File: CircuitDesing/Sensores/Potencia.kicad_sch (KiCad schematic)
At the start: 5 parts

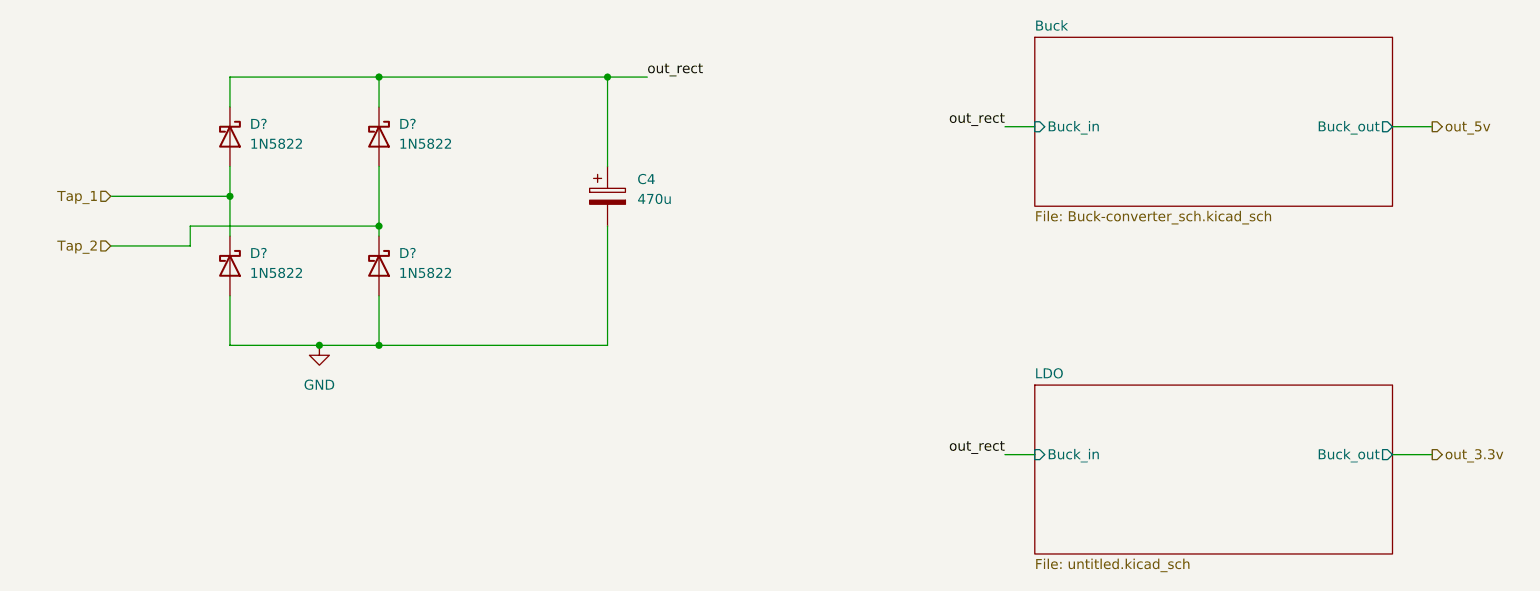
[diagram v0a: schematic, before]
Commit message: Modificaciones generales
Modificaciones a esquemático,  interacción con otros grupos, sistema de potencia.
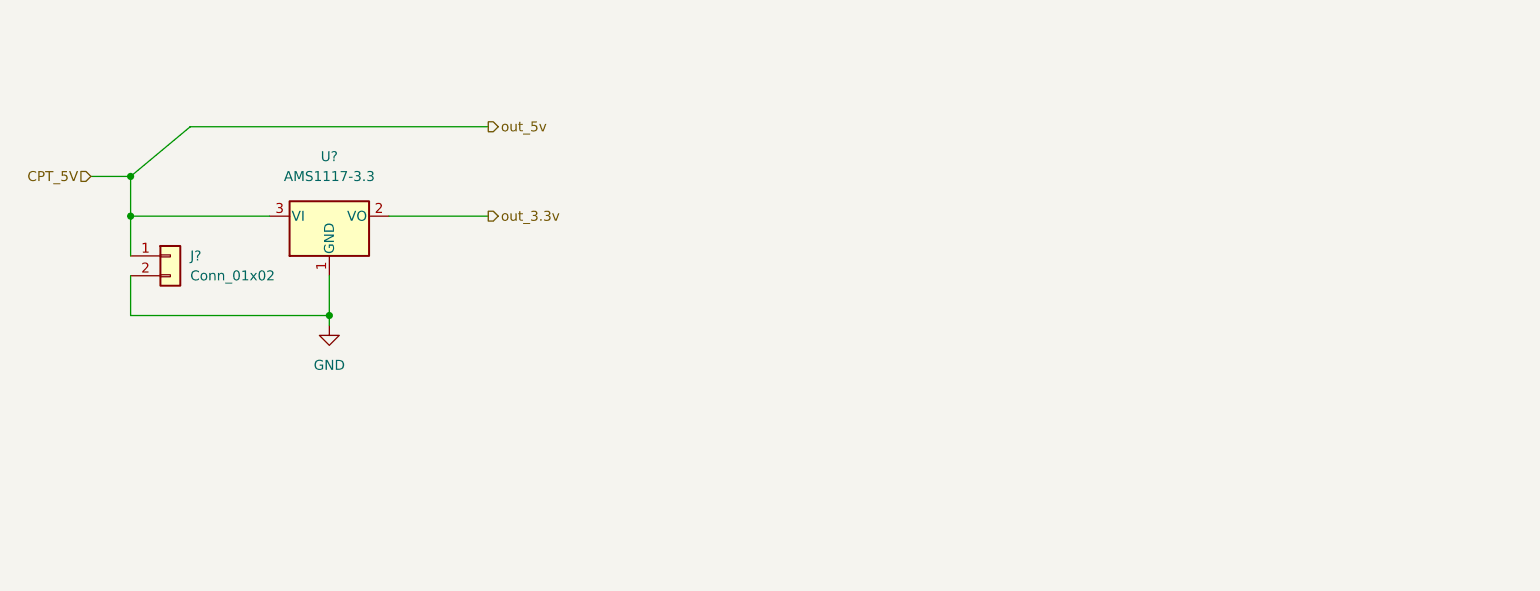
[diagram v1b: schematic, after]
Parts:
- removed C4: 470u, symbol Device:C_Polarized
- removed D? (x4): 1N5822, Diode_THT:D_DO-201AD_P15.24mm_Horizontal, symbol Diode:1N5822
- added J?: Conn_01x02, symbol Connector_Generic:Conn_01x02
- added U?: AMS1117-3.3, Package_TO_SOT_SMD:SOT-223-3_TabPin2, symbol Regulator_Linear:AMS1117-3.3
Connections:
- net GND: now also J?.2 (Pin_2), U?.1 (GND)
- net out_3.3v: now also U?.2 (VO)
- new net CPT_5V: J?.1 (Pin_1), U?.3 (VI)
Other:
- removed sheet Buck
- removed sheet LDO

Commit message: Huellas
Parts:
- J1: renamed from J?; footprint (none) -> TerminalBlock:TerminalBlock_bornier-2_P5.08mm
- gave numbers to parts that had none: 1
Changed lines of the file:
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@@
   (symbol (lib_id "Connector_Generic:Conn_01x02") (at 59.69 73.66 0) (unit 1)
     (in_bom yes) (on_board yes) (fields_autoplaced)
-    (property "Reference" "J?" (id 0) (at 62.23 73.6599 0)
+    (property "Reference" "J1" (id 0) (at 62.23 73.6599 0)
       (effects (font (size 1.27 1.27)) (justify left))
     )
@@
       (effects (font (size 1.27 1.27)) (justify left))
     )
-    (property "Footprint" "" (id 2) (at 59.69 73.66 0)
+    (property "Footprint" "TerminalBlock:TerminalBlock_bornier-2_P5.08mm" (id 2) (at 59.69 73.66 0)
       (effects (font (size 1.27 1.27)) hide)
     )
@@
   (symbol (lib_id "Regulator_Linear:AMS1117-3.3") (at 80.01 68.58 0) (unit 1)
     (in_bom yes) (on_board yes) (fields_autoplaced)
-    (property "Reference" "U?" (id 0) (at 80.01 60.96 0))
+    (property "Reference" "U2" (id 0) (at 80.01 60.96 0))
     (property "Value" "AMS1117-3.3" (id 1) (at 80.01 63.5 0))
     (property "Footprint" "Package_TO_SOT_SMD:SOT-223-3_TabPin2" (id 2) (at 80.01 63.5 0)
@@
   (symbol (lib_id "power:GND") (at 80.01 82.55 0) (unit 1)
     (in_bom yes) (on_board yes) (fields_autoplaced)
-    (property "Reference" "#PWR?" (id 0) (at 80.01 88.9 0)
+    (property "Reference" "#PWR0110" (id 0) (at 80.01 88.9 0)
       (effects (font (size 1.27 1.27)) hide)
     )

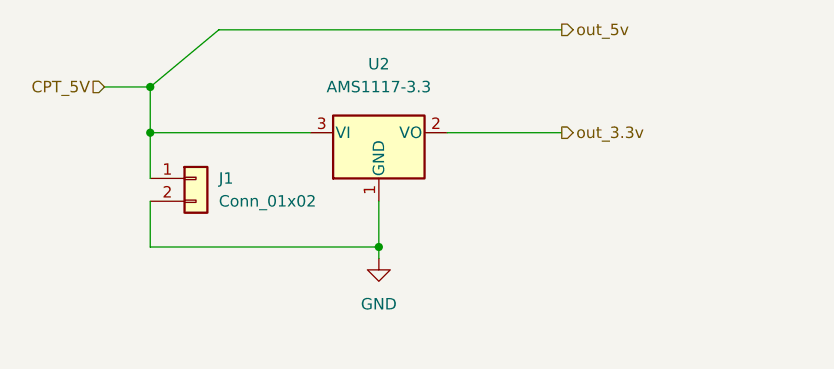
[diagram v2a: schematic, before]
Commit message: Condensadores LDO
Condensadores LDO
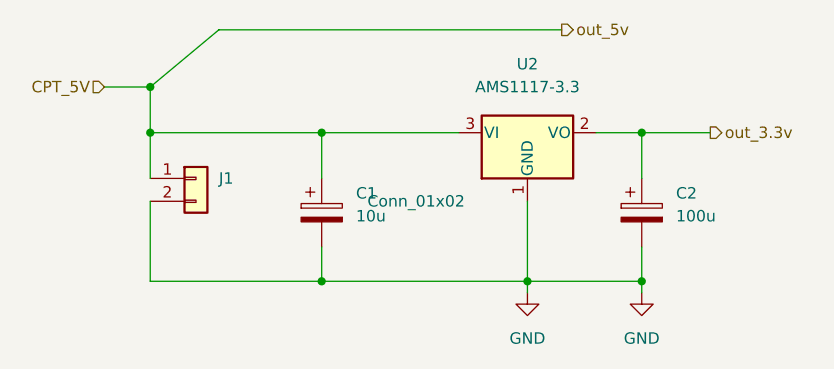
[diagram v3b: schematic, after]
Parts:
- added C1: 10u, Capacitor_SMD:C_0603_1608Metric_Pad1.08x0.95mm_HandSolder, symbol Device:C_Polarized
- added C2: 100u, Capacitor_SMD:C_0603_1608Metric_Pad1.08x0.95mm_HandSolder, symbol Device:C_Polarized
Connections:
- net CPT_5V: now also C1.1
- net GND: now also C1.2, C2.2
- net out_3.3v: now also C2.1
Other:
- moved on the sheet: U2
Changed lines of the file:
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@@
 (kicad_sch (version 20211123) (generator eeschema)
   (paper "A4")
-  (junction (at 80.01 81.28) (diameter 0) (color 0 0 0 0)
+  (junction (at 109.22 85.09) (diameter 0) (color 0 0 0 0)
   )
   (junction (at 54.61 63.5) (diameter 0) (color 0 0 0 0)
   )
+  (junction (at 73.66 68.58) (diameter 0) (color 0 0 0 0)
+  )
+  (junction (at 96.52 85.09) (diameter 0) (color 0 0 0 0)
+  )
+  (junction (at 73.66 85.09) (diameter 0) (color 0 0 0 0)
+  )
+  (junction (at 109.22 68.58) (diameter 0) (color 0 0 0 0)
+  )
   (junction (at 54.61 68.58) (diameter 0) (color 0 0 0 0)
   )
-  (wire (pts (xy 54.61 68.58) (xy 72.39 68.58))
+  (wire (pts (xy 96.52 76.2) (xy 96.52 85.09))
     (stroke (width 0) (type default) (color 0 0 0 0))
   )
-  (wire (pts (xy 80.01 76.2) (xy 80.01 81.28))
+  (wire (pts (xy 109.22 68.58) (xy 116.84 68.58))
     (stroke (width 0) (type default) (color 0 0 0 0))
   )
-  (wire (pts (xy 54.61 76.2) (xy 54.61 81.28))
+  (wire (pts (xy 54.61 76.2) (xy 54.61 85.09))
     (stroke (width 0) (type default) (color 0 0 0 0))
   )
-  (wire (pts (xy 80.01 81.28) (xy 54.61 81.28))
+  (wire (pts (xy 54.61 68.58) (xy 73.66 68.58))
+    (stroke (width 0) (type default) (color 0 0 0 0))
+  )
+  (wire (pts (xy 73.66 85.09) (xy 54.61 85.09))
+    (stroke (width 0) (type default) (color 0 0 0 0))
+  )
+  (wire (pts (xy 73.66 68.58) (xy 88.9 68.58))
     (stroke (width 0) (type default) (color 0 0 0 0))
   )
@@
     (stroke (width 0) (type default) (color 0 0 0 0))
   )
-  (wire (pts (xy 87.63 68.58) (xy 100.33 68.58))
+  (wire (pts (xy 109.22 68.58) (xy 109.22 73.66))
+    (stroke (width 0) (type default) (color 0 0 0 0))
+  )
+  (wire (pts (xy 96.52 85.09) (xy 96.52 86.36))
+    (stroke (width 0) (type default) (color 0 0 0 0))
+  )
+  (wire (pts (xy 104.14 68.58) (xy 109.22 68.58))
+    (stroke (width 0) (type default) (color 0 0 0 0))
+  )
+  (wire (pts (xy 73.66 68.58) (xy 73.66 73.66))
     (stroke (width 0) (type default) (color 0 0 0 0))
   )
   (wire (pts (xy 54.61 68.58) (xy 54.61 73.66))
-    (stroke (width 0) (type default) (color 0 0 0 0))
-  )
-  (wire (pts (xy 80.01 81.28) (xy 80.01 82.55))
     (stroke (width 0) (type default) (color 0 0 0 0))
   )
@@
   )
   (wire (pts (xy 62.23 57.15) (xy 54.61 63.5))
+    (stroke (width 0) (type default) (color 0 0 0 0))
+  )
+  (wire (pts (xy 109.22 85.09) (xy 109.22 81.28))
+    (stroke (width 0) (type default) (color 0 0 0 0))
+  )
+  (wire (pts (xy 96.52 85.09) (xy 109.22 85.09))
+    (stroke (width 0) (type default) (color 0 0 0 0))
+  )
+  (wire (pts (xy 109.22 86.36) (xy 109.22 85.09))
+    (stroke (width 0) (type default) (color 0 0 0 0))
+  )
+  (wire (pts (xy 73.66 85.09) (xy 96.52 85.09))
+    (stroke (width 0) (type default) (color 0 0 0 0))
+  )
+  (wire (pts (xy 73.66 81.28) (xy 73.66 85.09))
     (stroke (width 0) (type default) (color 0 0 0 0))
   )
@@
     (effects (font (size 1.27 1.27)) (justify left))
   )
-  (hierarchical_label "out_3.3v" (shape output) (at 100.33 68.58 0)
+  (hierarchical_label "out_3.3v" (shape output) (at 116.84 68.58 0)
     (effects (font (size 1.27 1.27)) (justify left))
   )
+  (symbol (lib_id "power:GND") (at 109.22 86.36 0) (unit 1)
+    (in_bom yes) (on_board yes) (fields_autoplaced)
+    (property "Reference" "#PWR?" (id 0) (at 109.22 92.71 0)
+      (effects (font (size 1.27 1.27)) hide)
+    )
+    (property "Value" "GND" (id 1) (at 109.22 91.44 0))
+    (property "Footprint" "" (id 2) (at 109.22 86.36 0)
+      (effects (font (size 1.27 1.27)) hide)
+    )
+    (property "Datasheet" "" (id 3) (at 109.22 86.36 0)
+      (effects (font (size 1.27 1.27)) hide)
+    )
+    (pin "1")
+  )
+  (symbol (lib_id "Device:C_Polarized") (at 109.22 77.47 0) (unit 1)
+    (in_bom yes) (on_board yes) (fields_autoplaced)
+    (property "Reference" "C2" (id 0) (at 113.03 75.3109 0)
+      (effects (font (size 1.27 1.27)) (justify left))
+    )
+    (property "Value" "100u" (id 1) (at 113.03 77.8509 0)
+      (effects (font (size 1.27 1.27)) (justify left))
+    )
+    (property "Footprint" "Capacitor_SMD:C_0603_1608Metric_Pad1.08x0.95mm_HandSolder" (id 2) (at 110.1852 81.28 0)
+      (effects (font (size 1.27 1.27)) hide)
+    )
+    (property "Datasheet" "~" (id 3) (at 109.22 77.47 0)
+      (effects (font (size 1.27 1.27)) hide)
+    )
+    (pin "1")
+    (pin "2")
+  )
   (symbol (lib_id "Connector_Generic:Conn_01x02") (at 59.69 73.66 0) (unit 1)
-    (in_bom yes) (on_board yes) (fields_autoplaced)
+    (in_bom yes) (on_board yes)
     (property "Reference" "J1" (id 0) (at 62.23 73.6599 0)
       (effects (font (size 1.27 1.27)) (justify left))
     )
-    (property "Value" "Conn_01x02" (id 1) (at 62.23 76.1999 0)
+    (property "Value" "Conn_01x02" (id 1) (at 78.74 76.1999 0)
       (effects (font (size 1.27 1.27)) (justify left))
     )
@@
     (pin "2")
   )
-  (symbol (lib_id "Regulator_Linear:AMS1117-3.3") (at 80.01 68.58 0) (unit 1)
+  (symbol (lib_id "Device:C_Polarized") (at 73.66 77.47 0) (unit 1)
     (in_bom yes) (on_board yes) (fields_autoplaced)
-    (property "Reference" "U2" (id 0) (at 80.01 60.96 0))
-    (property "Value" "AMS1117-3.3" (id 1) (at 80.01 63.5 0))
-    (property "Footprint" "Package_TO_SOT_SMD:SOT-223-3_TabPin2" (id 2) (at 80.01 63.5 0)
+    (property "Reference" "C1" (id 0) (at 77.47 75.3109 0)
+      (effects (font (size 1.27 1.27)) (justify left))
+    )
+    (property "Value" "10u" (id 1) (at 77.47 77.8509 0)
+      (effects (font (size 1.27 1.27)) (justify left))
+    )
+    (property "Footprint" "Capacitor_SMD:C_0603_1608Metric_Pad1.08x0.95mm_HandSolder" (id 2) (at 74.6252 81.28 0)
       (effects (font (size 1.27 1.27)) hide)
     )
-    (property "Datasheet" "http://www.advanced-monolithic.com/pdf/ds1117.pdf" (id 3) (at 82.55 74.93 0)
+    (property "Datasheet" "~" (id 3) (at 73.66 77.47 0)
+      (effects (font (size 1.27 1.27)) hide)
+    )
+    (pin "1")
+    (pin "2")
+  )
+  (symbol (lib_id "Regulator_Linear:AMS1117-3.3") (at 96.52 68.58 0) (unit 1)
+    (in_bom yes) (on_board yes) (fields_autoplaced)
+    (property "Reference" "U2" (id 0) (at 96.52 60.96 0))
+    (property "Value" "AMS1117-3.3" (id 1) (at 96.52 63.5 0))
+    (property "Footprint" "Package_TO_SOT_SMD:SOT-223-3_TabPin2" (id 2) (at 96.52 63.5 0)
+      (effects (font (size 1.27 1.27)) hide)
+    )
+    (property "Datasheet" "http://www.advanced-monolithic.com/pdf/ds1117.pdf" (id 3) (at 99.06 74.93 0)
       (effects (font (size 1.27 1.27)) hide)
     )
@@
     (pin "3")
   )
-  (symbol (lib_id "power:GND") (at 80.01 82.55 0) (unit 1)
+  (symbol (lib_id "power:GND") (at 96.52 86.36 0) (unit 1)
     (in_bom yes) (on_board yes) (fields_autoplaced)
-    (property "Reference" "#PWR0110" (id 0) (at 80.01 88.9 0)
+    (property "Reference" "#PWR0110" (id 0) (at 96.52 92.71 0)
       (effects (font (size 1.27 1.27)) hide)
     )
-    (property "Value" "GND" (id 1) (at 80.01 87.63 0))
-    (property "Footprint" "" (id 2) (at 80.01 82.55 0)
+    (property "Value" "GND" (id 1) (at 96.52 91.44 0))
+    (property "Footprint" "" (id 2) (at 96.52 86.36 0)
       (effects (font (size 1.27 1.27)) hide)
     )
-    (property "Datasheet" "" (id 3) (at 80.01 82.55 0)
+    (property "Datasheet" "" (id 3) (at 96.52 86.36 0)
       (effects (font (size 1.27 1.27)) hide)
     )

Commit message: Ruteo2.0
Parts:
- renumbered C1 to C5, C2 to C6, J1 to J2
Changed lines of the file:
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@@
   (symbol (lib_id "power:GND") (at 109.22 86.36 0) (unit 1)
     (in_bom yes) (on_board yes) (fields_autoplaced)
-    (property "Reference" "#PWR?" (id 0) (at 109.22 92.71 0)
+    (property "Reference" "#PWR021" (id 0) (at 109.22 92.71 0)
       (effects (font (size 1.27 1.27)) hide)
     )
@@
   (symbol (lib_id "Device:C_Polarized") (at 109.22 77.47 0) (unit 1)
     (in_bom yes) (on_board yes) (fields_autoplaced)
-    (property "Reference" "C2" (id 0) (at 113.03 75.3109 0)
+    (property "Reference" "C6" (id 0) (at 113.03 75.3109 0)
       (effects (font (size 1.27 1.27)) (justify left))
     )
@@
   (symbol (lib_id "Connector_Generic:Conn_01x02") (at 59.69 73.66 0) (unit 1)
     (in_bom yes) (on_board yes)
-    (property "Reference" "J1" (id 0) (at 62.23 73.6599 0)
+    (property "Reference" "J2" (id 0) (at 62.23 73.6599 0)
       (effects (font (size 1.27 1.27)) (justify left))
     )
@@
   (symbol (lib_id "Device:C_Polarized") (at 73.66 77.47 0) (unit 1)
     (in_bom yes) (on_board yes) (fields_autoplaced)
-    (property "Reference" "C1" (id 0) (at 77.47 75.3109 0)
+    (property "Reference" "C5" (id 0) (at 77.47 75.3109 0)
       (effects (font (size 1.27 1.27)) (justify left))
     )
@@
   (symbol (lib_id "power:GND") (at 96.52 86.36 0) (unit 1)
     (in_bom yes) (on_board yes) (fields_autoplaced)
-    (property "Reference" "#PWR0110" (id 0) (at 96.52 92.71 0)
+    (property "Reference" "#PWR020" (id 0) (at 96.52 92.71 0)
       (effects (font (size 1.27 1.27)) hide)
     )
